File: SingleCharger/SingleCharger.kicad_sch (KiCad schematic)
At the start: 7 parts, among them U2 PICO

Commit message: Rebuild
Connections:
- net +3V3: now also U2.36 (3V3(OUT))
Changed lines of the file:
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@@
+	(wire
+		(pts
+			(xy 186.69 81.28) (xy 171.45 81.28)
+		)
+		(stroke
+			(width 0)
+			(type default)
+		)
+	)
 	(wire
 		(pts
@@
 					(unit 1)
 				)
+			)
+		)
+	)
+	(symbol
+		(lib_id "power:+3V3")
+		(at 186.69 81.28 270)
+		(unit 1)
+		(exclude_from_sim no)
+		(in_bom yes)
+		(on_board yes)
+		(dnp no)
+		(fields_autoplaced yes)
+		(property "Reference" "#PWR057"
+			(at 182.88 81.28 0)
+			(effects
+				(font
+					(size 1.27 1.27)
+				)
+				(hide yes)
+			)
+		)
+		(property "Value" "+3V3"
+			(at 190.5 81.2799 90)
+			(effects
+				(font
+					(size 1.27 1.27)
+				)
+				(justify left)
+			)
+		)
+		(property "Footprint" ""
+			(at 186.69 81.28 0)
+			(effects
+				(font
+					(size 1.27 1.27)
+				)
+				(hide yes)
+			)
+		)
+		(property "Datasheet" ""
+			(at 186.69 81.28 0)
+			(effects
+				(font
+					(size 1.27 1.27)
+				)
+				(hide yes)
+			)
+		)
+		(property "Description" "Power symbol creates a global label with name \"+3V3\""
+			(at 186.69 81.28 0)
+			(effects
+				(font
+					(size 1.27 1.27)
+				)
+				(hide yes)
+			)
+		)
+		(pin "1"
+		)
+		(instances
+			(project "SingleCharger"
+				(path "/e710e346-5907-4662-9fec-fc15df74dc9e"
+					(reference "#PWR057")
+					(unit 1)
+				)

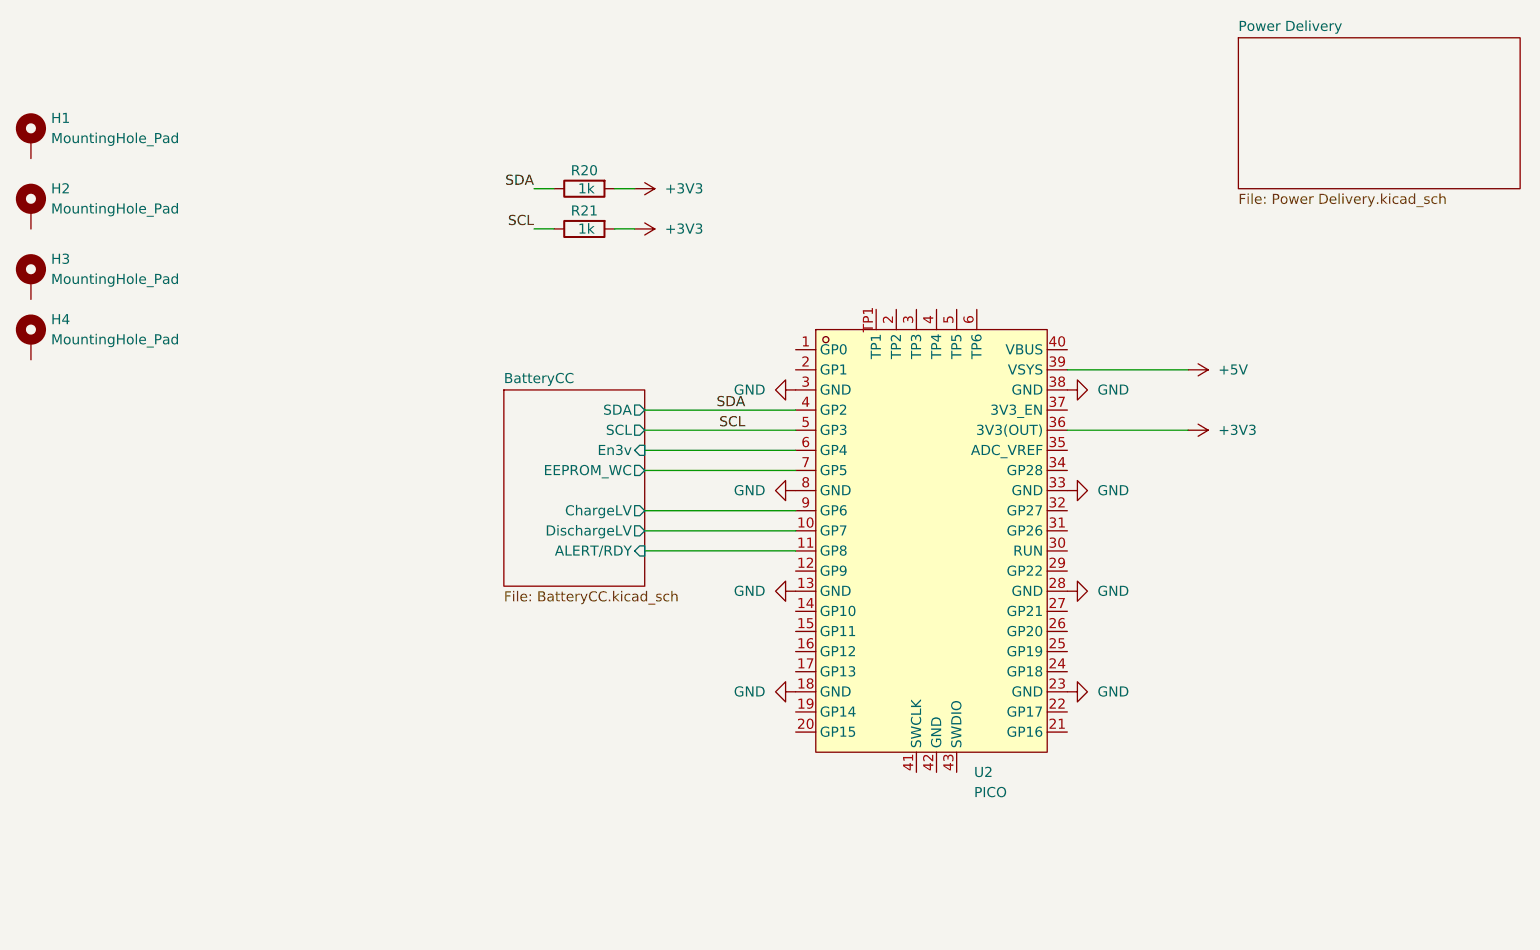
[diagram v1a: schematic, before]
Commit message: Moved to +48V Feed. 25.2 Controlled by Pico.
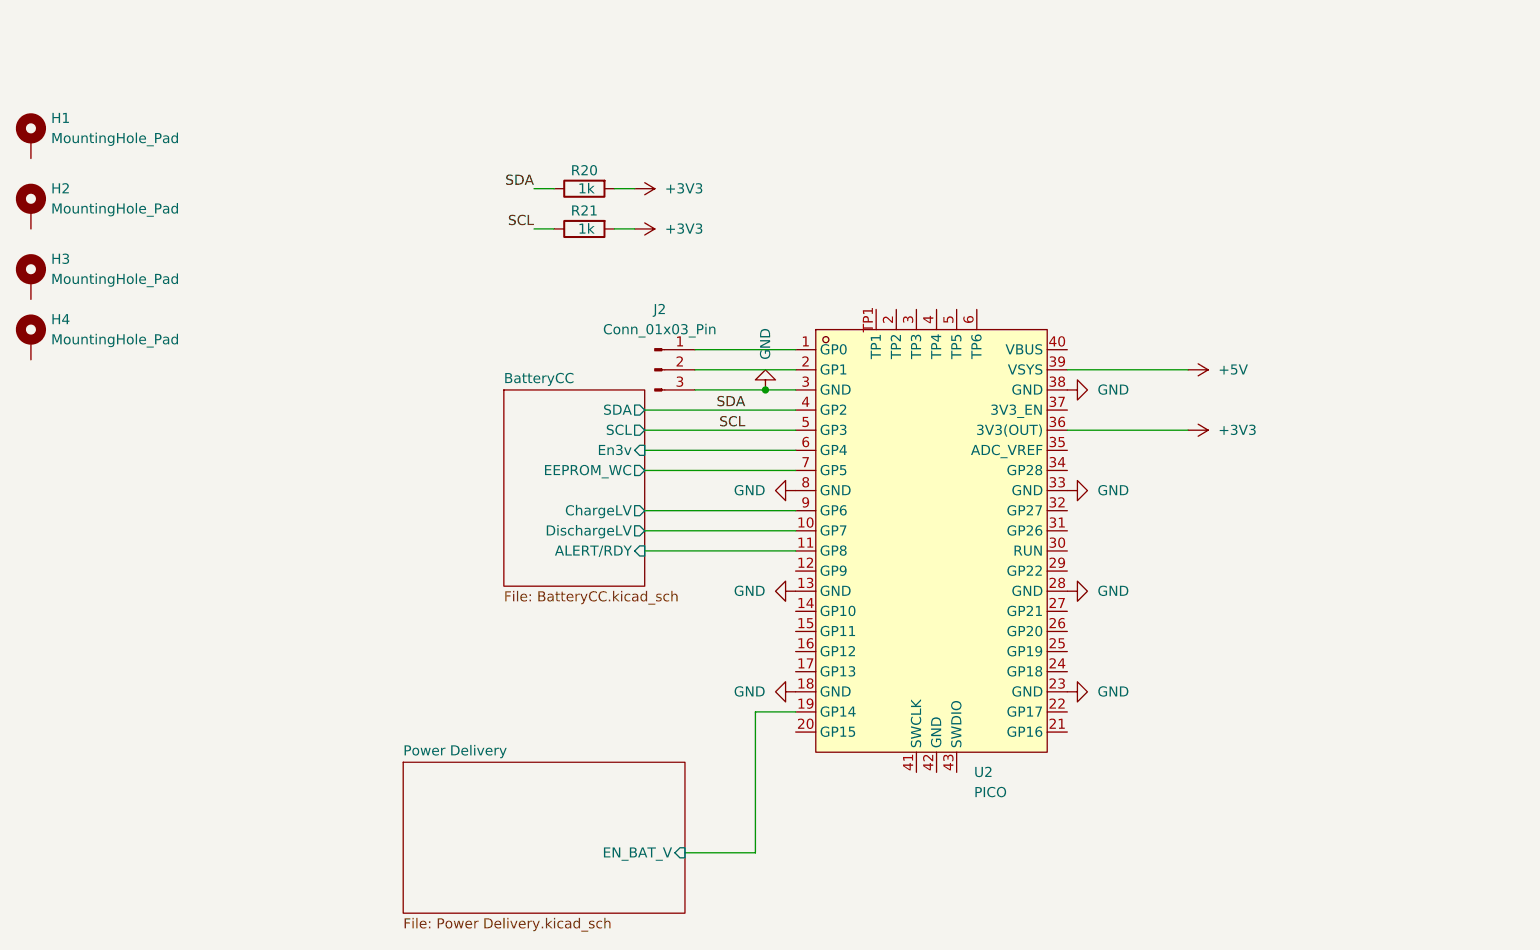
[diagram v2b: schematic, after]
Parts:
- added J2: Conn_01x03_Pin, Connector_PinHeader_2.54mm:PinHeader_1x03_P2.54mm_Vertical, symbol Connector:Conn_01x03_Pin
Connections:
- net GND: now also J2.3 (Pin_3)
- net at U2.1 (GP0): now also J2.1 (Pin_1)
- net Power Delivery/EN_BAT_V: now reaches U2.19 (GP14)
- new net: J2.2 (Pin_2), U2.2 (TP2)
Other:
- sheet Power Delivery ports: added EN_BAT_V; removed none
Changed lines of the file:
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@@
 	(generator_version "9.0")
 	(paper "A4")
+	(junction
+		(at 133.35 76.2)
+		(diameter 0)
+		(color 0 0 0 0)
+	)
 	(wire
 		(pts
@@
 	(wire
 		(pts
+			(xy 132.08 134.62) (xy 123.19 134.62)
+		)
+		(stroke
+			(width 0)
+			(type default)
+		)
+	)
+	(wire
+		(pts
 			(xy 118.11 91.44) (xy 137.16 91.44)
 		)
@@
 	(wire
 		(pts
+			(xy 124.46 71.12) (xy 137.16 71.12)
+		)
+		(stroke
+			(width 0)
+			(type default)
+		)
+	)
+	(wire
+		(pts
 			(xy 118.11 86.36) (xy 137.16 86.36)
 		)
@@
 	(wire
 		(pts
+			(xy 132.08 116.84) (xy 132.08 134.62)
+		)
+		(stroke
+			(width 0)
+			(type default)
+		)
+	)
+	(wire
+		(pts
+			(xy 124.46 76.2) (xy 133.35 76.2)
+		)
+		(stroke
+			(width 0)
+			(type default)
+		)
+	)
+	(wire
+		(pts
+			(xy 124.46 73.66) (xy 137.16 73.66)
+		)
+		(stroke
+			(width 0)
+			(type default)
+		)
+	)
+	(wire
+		(pts
 			(xy 118.11 81.28) (xy 137.16 81.28)
 		)
@@
 	(wire
 		(pts
+			(xy 133.35 76.2) (xy 137.16 76.2)
+		)
+		(stroke
+			(width 0)
+			(type default)
+		)
+	)
+	(wire
+		(pts
 			(xy 118.11 93.98) (xy 137.16 93.98)
+		)
+		(stroke
+			(width 0)
+			(type default)
+		)
+	)
+	(wire
+		(pts
+			(xy 137.16 116.84) (xy 132.08 116.84)
 		)
 		(stroke
@@
 	)
 	(symbol
-		(lib_id "power:GND")
-		(at 137.16 76.2 270)
-		(mirror x)
+		(lib_id "Connector:Conn_01x03_Pin")
+		(at 119.38 73.66 0)
 		(unit 1)
 		(exclude_from_sim no)
@@
 		(on_board yes)
 		(dnp no)
+		(fields_autoplaced yes)
+		(property "Reference" "J2"
+			(at 120.015 66.04 0)
+			(effects
+				(font
+					(size 1.27 1.27)
+				)
+			)
+		)
+		(property "Value" "Conn_01x03_Pin"
+			(at 120.015 68.58 0)
+			(effects
+				(font
+					(size 1.27 1.27)
+				)
+			)
+		)
+		(property "Footprint" "Connector_PinHeader_2.54mm:PinHeader_1x03_P2.54mm_Vertical"
+			(at 119.38 73.66 0)
+			(effects
+				(font
+					(size 1.27 1.27)
+				)
+				(hide yes)
+			)
+		)
+		(property "Datasheet" "~"
+			(at 119.38 73.66 0)
+			(effects
+				(font
+					(size 1.27 1.27)
+				)
+				(hide yes)
+			)
+		)
+		(property "Description" "Generic connector, single row, 01x03, script generated"
+			(at 119.38 73.66 0)
+			(effects
+				(font
+					(size 1.27 1.27)
+				)
+				(hide yes)
+			)
+		)
+		(pin "1"
+		)
+		(pin "2"
+		)
+		(pin "3"
+		)
+		(instances
+			(project ""
+				(path "/e710e346-5907-4662-9fec-fc15df74dc9e"
+					(reference "J2")
+					(unit 1)
+				)
+			)
+		)
+	)
+	(symbol
+		(lib_id "power:GND")
+		(at 133.35 76.2 0)
+		(mirror x)
+		(unit 1)
+		(exclude_from_sim no)
+		(in_bom yes)
+		(on_board yes)
+		(dnp no)
 		(property "Reference" "#PWR048"
-			(at 130.81 76.2 0)
+			(at 133.35 69.85 0)
 			(effects
 				(font
@@
 		)
 		(property "Value" "GND"
-			(at 133.35 76.1999 90)
+			(at 133.3501 72.39 90)
 			(effects
 				(font
@@
 		)
 		(property "Footprint" ""
-			(at 137.16 76.2 0)
+			(at 133.35 76.2 0)
 			(effects
 				(font
@@
 		)
 		(property "Datasheet" ""
-			(at 137.16 76.2 0)
+			(at 133.35 76.2 0)
 			(effects
 				(font
@@
 		)
 		(property "Description" "Power symbol creates a global label with name \"GND\" , ground"
-			(at 137.16 76.2 0)
+			(at 133.35 76.2 0)
 			(effects
 				(font
@@
 	)
 	(sheet
-		(at 193.04 31.75)
+		(at 87.63 123.19)
 		(size 35.56 19.05)
 		(exclude_from_sim no)
@@
 		)
 		(property "Sheetname" "Power Delivery"
-			(at 193.04 31.0384 0)
+			(at 87.63 122.4784 0)
 			(effects
 				(font
@@
 		)
 		(property "Sheetfile" "Power Delivery.kicad_sch"
-			(at 193.04 51.3846 0)
+			(at 87.63 142.8246 0)
 			(effects
 				(font
@@
 			)
 		)
+		(pin "EN_BAT_V" input
+			(at 123.19 134.62 0)
+			(effects
+				(font
+					(size 1.27 1.27)
+				)
+				(justify right)
+			)
+		)

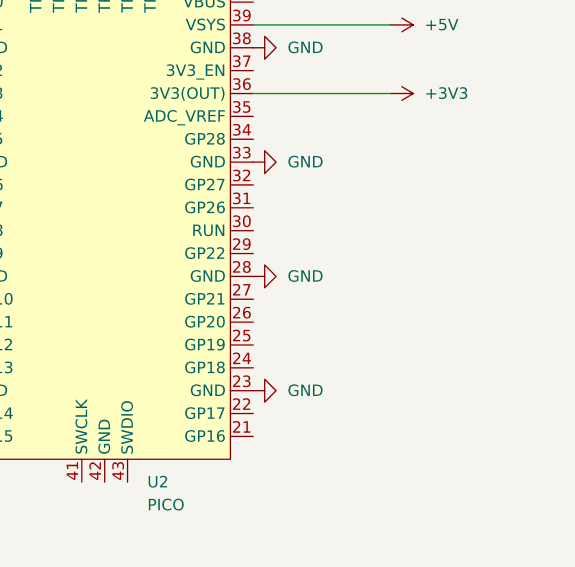
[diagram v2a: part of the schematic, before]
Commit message: Added SCL/SDA Pins.
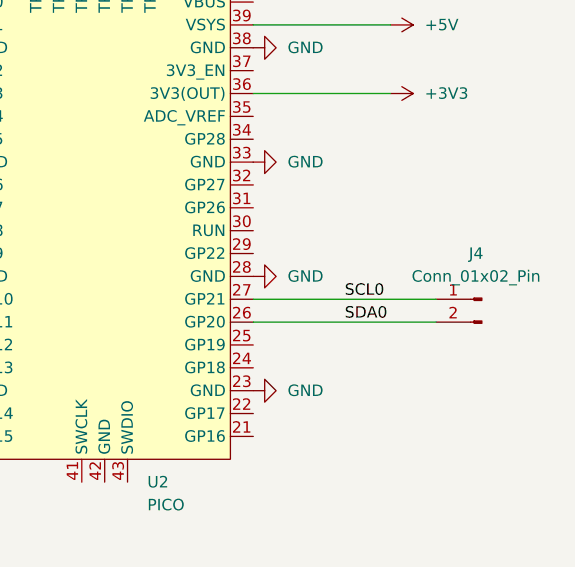
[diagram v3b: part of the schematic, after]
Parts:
- added J4: Conn_01x02_Pin, Connector_PinHeader_2.54mm:PinHeader_1x02_P2.54mm_Vertical, symbol Connector:Conn_01x02_Pin
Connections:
- net SDA0: now reaches U2.26 (GP20)
- net SDA0: now also J4.2 (Pin_2)
- net SCL0: now reaches U2.27 (GP21)
- net SCL0: now also J4.1 (Pin_1)
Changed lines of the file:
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@@
+	(wire
+		(pts
+			(xy 191.77 106.68) (xy 171.45 106.68)
+		)
+		(stroke
+			(width 0)
+			(type default)
+		)
+	)
 	(wire
 		(pts
 			(xy 186.69 81.28) (xy 171.45 81.28)
+		)
+		(stroke
+			(width 0)
+			(type default)
+		)
+	)
+	(wire
+		(pts
+			(xy 191.77 104.14) (xy 171.45 104.14)
 		)
 		(stroke
@@
 		)
 	)
+	(label "SDA0"
+		(at 181.61 106.68 0)
+		(effects
+			(font
+				(size 1.27 1.27)
+			)
+			(justify left bottom)
+		)
+	)
 	(label "SDA"
 		(at 130.81 78.74 180)
@@
 		)
 	)
+	(label "SCL0"
+		(at 181.61 104.14 0)
+		(effects
+			(font
+				(size 1.27 1.27)
+			)
+			(justify left bottom)
+		)
+	)
 	(symbol
 		(lib_id "Device:R")
@@
 					(unit 1)
 				)
+			)
+		)
+	)
+	(symbol
+		(lib_id "Connector:Conn_01x02_Pin")
+		(at 196.85 104.14 0)
+		(mirror y)
+		(unit 1)
+		(exclude_from_sim no)
+		(in_bom yes)
+		(on_board yes)
+		(dnp no)
+		(property "Reference" "J4"
+			(at 196.215 99.06 0)
+			(effects
+				(font
+					(size 1.27 1.27)
+				)
+			)
+		)
+		(property "Value" "Conn_01x02_Pin"
+			(at 196.215 101.6 0)
+			(effects
+				(font
+					(size 1.27 1.27)
+				)
+			)
+		)
+		(property "Footprint" "Connector_PinHeader_2.54mm:PinHeader_1x02_P2.54mm_Vertical"
+			(at 196.85 104.14 0)
+			(effects
+				(font
+					(size 1.27 1.27)
+				)
+				(hide yes)
+			)
+		)
+		(property "Datasheet" "~"
+			(at 196.85 104.14 0)
+			(effects
+				(font
+					(size 1.27 1.27)
+				)
+				(hide yes)
+			)
+		)
+		(property "Description" "Generic connector, single row, 01x02, script generated"
+			(at 196.85 104.14 0)
+			(effects
+				(font
+					(size 1.27 1.27)
+				)
+				(hide yes)
+			)
+		)
+		(pin "2"
+		)
+		(pin "1"
+		)
+		(instances
+			(project "SingleCharger"
+				(path "/e710e346-5907-4662-9fec-fc15df74dc9e"
+					(reference "J4")
+					(unit 1)
+				)
